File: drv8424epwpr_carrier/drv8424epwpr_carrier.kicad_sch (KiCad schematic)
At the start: 26 parts, among them J4 Conn_01x08, J5 Conn_01x08, U1 DRV8424EPWPR, U2 DMP4013LFG-7

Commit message: add footprint
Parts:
- CR1: footprint SOD123_DIO -> MMSZ5245B_7_F:SOD123_DIO
- C_SW1: renamed from C_SW; footprint CAPC340180_88N_KEM -> C1206C223J8RACTU:CAPC340180_88N_KEM
- C_VCP1: renamed from C_VCP; footprint CAPC340180_100N_KEM -> C1206C224K4RACTU:CAPC340180_100N_KEM
- C_VM1, C_VM2: footprint CAPC220145_88N_KEM -> C0805C103K8RACTU:CAPC220145_88N_KEM
- C_VM3, C_VM4: footprint EEE0GA101SR -> EEE-1AA101WR:EEE0GA101SR
- J4, J5: footprint (none) -> Connector_PinHeader_2.54mm:PinHeader_1x08_P2.54mm_Vertical
- LED1: footprint APHCM2012SYCK-F01:LED_APHCM2012SYCK-F01 -> APHCM2012SYCK_F01:LED_APHCM2012SYCK-F01
- LED2, LED4: footprint LED_APHCM2012CGCK-F01_KNB -> APHCM2012CGCK_F01:LED_APHCM2012CGCK-F01_KNB
- LED3, LED5: footprint APHCM2012SURCK-F01:LED_APHCM2012SURCK-F01 -> APHCM2012SURCK_F01:LED_APHCM2012SURCK-F01
- R1: footprint RC1206N_YAG -> RC1206FR_07100KL:RC1206N_YAG
- R1_REFA1: renamed from R1_REFA; footprint RC1206N_YAG -> RC1206FR_0747KL:RC1206N_YAG
- R1_REFB1: renamed from R1_REFB; footprint RC1206N_YAG -> RC1206FR_0747KL:RC1206N_YAG
- R2, R3, R4: footprint RC1206N_YAG -> RC1206FR_07590RL:RC1206N_YAG
- R2_REFA1: renamed from R2_REFA; footprint RC1206N_YAG -> RC1206FR_0716KL:RC1206N_YAG
- R2_REFB1: renamed from R2_REFB; footprint RC1206N_YAG -> RC1206FR_0716KL:RC1206N_YAG
- R_nFAULT1: renamed from R_nFAULT; footprint RC1206N_YAG -> RC1206FR_0710KL:RC1206N_YAG
- U1: footprint HTSSOP28_PWP_TEX -> DRV8424EPWPR:HTSSOP28_PWP_TEX
- U2: footprint SON8_DMP4013LFG-7_DIO -> DMP4013LFG_7:SON8_DMP4013LFG-7_DIO
- renumbered C_DVDD to C_DVDD1
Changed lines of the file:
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@@
 	(wire
 		(pts
+			(xy 124.46 80.01) (xy 124.46 78.74)
+		)
+		(stroke
+			(width 0)
+			(type default)
+		)
+	)
+	(wire
+		(pts
 			(xy 93.98 39.37) (xy 93.98 58.42)
 		)
@@
 			)
 		)
-		(property "Footprint" ""
+		(property "Footprint" "Connector_PinHeader_2.54mm:PinHeader_1x08_P2.54mm_Vertical"
 			(at 190.5 45.72 0)
 			(effects
@@
 			)
 		)
-		(property "Footprint" "LED_APHCM2012CGCK-F01_KNB"
+		(property "Footprint" "APHCM2012CGCK_F01:LED_APHCM2012CGCK-F01_KNB"
 			(at 58.42 125.73 0)
 			(effects
@@
 			)
 		)
-		(property "Footprint" "RC1206N_YAG"
+		(property "Footprint" "RC1206FR_07590RL:RC1206N_YAG"
 			(at 44.45 97.79 0)
 			(effects
@@
 		(dnp no)
 		(fields_autoplaced yes)
-		(property "Reference" "R2_REFB"
+		(property "Reference" "R2_REFB1"
 			(at 261.62 129.5399 90)
 			(effects
@@
 			)
 		)
-		(property "Footprint" "RC1206N_YAG"
+		(property "Footprint" "RC1206FR_0716KL:RC1206N_YAG"
 			(at 259.08 137.16 0)
 			(effects
@@
 			(project "drv8424epwpr_carrier"
 				(path "/ffaa5cf3-cedd-4f84-9f10-7046972ed335"
-					(reference "R2_REFB")
+					(reference "R2_REFB1")
 					(unit 1)
 				)
@@
 			)
 		)
-		(property "Footprint" "CAPC220145_88N_KEM"
+		(property "Footprint" "C0805C103K8RACTU:CAPC220145_88N_KEM"
 			(at 124.46 49.53 0)
 			(effects
@@
 			)
 		)
-		(property "Footprint" "EEE0GA101SR"
+		(property "Footprint" "EEE-1AA101WR:EEE0GA101SR"
 			(at -2.21 67.31 0)
 			(effects
@@
 			)
 		)
-		(property "Footprint" "EEE0GA101SR"
+		(property "Footprint" "EEE-1AA101WR:EEE0GA101SR"
 			(at 9.22 55.88 0)
 			(effects
@@
 		(dnp no)
 		(fields_autoplaced yes)
-		(property "Reference" "C_VCP"
+		(property "Reference" "C_VCP1"
 			(at 113.03 93.98 0)
 			(effects
@@
 			)
 		)
-		(property "Footprint" "CAPC340180_100N_KEM"
+		(property "Footprint" "C1206C224K4RACTU:CAPC340180_100N_KEM"
 			(at 116.84 100.33 0)
 			(effects
@@
 			(project ""
 				(path "/ffaa5cf3-cedd-4f84-9f10-7046972ed335"
-					(reference "C_VCP")
+					(reference "C_VCP1")
 					(unit 1)
 				)
@@
 			)
 		)
-		(property "Footprint" "APHCM2012SYCK-F01:LED_APHCM2012SYCK-F01"
+		(property "Footprint" "APHCM2012SYCK_F01:LED_APHCM2012SYCK-F01"
 			(at 135.89 50.8 0)
 			(effects
@@
 	(symbol
 		(lib_id "power:GND")
-		(at 124.46 78.74 0)
+		(at 124.46 80.01 0)
 		(unit 1)
 		(exclude_from_sim no)
@@
 		(fields_autoplaced yes)
 		(property "Reference" "#PWR08"
-			(at 124.46 85.09 0)
+			(at 124.46 86.36 0)
 			(effects
 				(font
@@
 		)
 		(property "Value" "GND"
-			(at 124.46 83.82 0)
+			(at 124.46 85.09 0)
 			(effects
 				(font
@@
 		)
 		(property "Footprint" ""
-			(at 124.46 78.74 0)
+			(at 124.46 80.01 0)
 			(effects
 				(font
@@
 		)
 		(property "Datasheet" ""
-			(at 124.46 78.74 0)
+			(at 124.46 80.01 0)
 			(effects
 				(font
@@
 		)
 		(property "Description" "Power symbol creates a global label with name \"GND\" , ground"
-			(at 124.46 78.74 0)
+			(at 124.46 80.01 0)
 			(effects
 				(font
@@
 			)
 		)
-		(property "Footprint" "HTSSOP28_PWP_TEX"
+		(property "Footprint" "DRV8424EPWPR:HTSSOP28_PWP_TEX"
 			(at 127 100.33 0)
 			(effects
@@
 			)
 		)
-		(property "Footprint" "SON8_DMP4013LFG-7_DIO"
+		(property "Footprint" "DMP4013LFG_7:SON8_DMP4013LFG-7_DIO"
 			(at 73.66 46.99 0)
 			(effects
@@
 		(on_board yes)
 		(dnp no)
-		(property "Reference" "C_DVDD"
+		(property "Reference" "C_DVDD1"
 			(at 167.894 142.494 90)
 			(effects
@@
 			(project ""
 				(path "/ffaa5cf3-cedd-4f84-9f10-7046972ed335"
-					(reference "C_DVDD")
+					(reference "C_DVDD1")
 					(unit 1)
 				)
@@
 			)
 		)
-		(property "Footprint" "SOD123_DIO"
+		(property "Footprint" "MMSZ5245B_7_F:SOD123_DIO"
 			(at 81.28 54.61 0)
 			(effects
@@
 			)
 		)
-		(property "Footprint" "RC1206N_YAG"
+		(property "Footprint" "RC1206FR_07590RL:RC1206N_YAG"
 			(at 44.45 125.73 0)
 			(effects
@@
 		(on_board yes)
 		(dnp no)
-		(property "Reference" "C_SW"
+		(property "Reference" "C_SW1"
 			(at 185.42 96.52 0)
 			(effects
@@
 			)
 		)
-		(property "Footprint" "CAPC340180_88N_KEM"
+		(property "Footprint" "C1206C223J8RACTU:CAPC340180_88N_KEM"
 			(at 181.61 102.87 0)
 			(effects
@@
 			(project ""
 				(path "/ffaa5cf3-cedd-4f84-9f10-7046972ed335"
-					(reference "C_SW")
+					(reference "C_SW1")
 					(unit 1)
 				)
@@
 		(dnp no)
 		(fields_autoplaced yes)
-		(property "Reference" "R1_REFA"
+		(property "Reference" "R1_REFA1"
 			(at 232.41 111.7599 90)
 			(effects
@@
 			)
 		)
-		(property "Footprint" "RC1206N_YAG"
+		(property "Footprint" "RC1206FR_0747KL:RC1206N_YAG"
 			(at 229.87 119.38 0)
 			(effects
@@
 			(project ""
 				(path "/ffaa5cf3-cedd-4f84-9f10-7046972ed335"
-					(reference "R1_REFA")
+					(reference "R1_REFA1")
 					(unit 1)
 				)
@@
 			)
 		)
-		(property "Footprint" "APHCM2012SURCK-F01:LED_APHCM2012SURCK-F01"
+		(property "Footprint" "APHCM2012SURCK_F01:LED_APHCM2012SURCK-F01"
 			(at 63.5 137.16 0)
 			(effects
@@
 			)
 		)
-		(property "Footprint" "RC1206N_YAG"
+		(property "Footprint" "RC1206FR_07590RL:RC1206N_YAG"
 			(at 135.89 73.66 0)
 			(effects
@@
 		(dnp no)
 		(fields_autoplaced yes)
-		(property "Reference" "R_nFAULT"
+		(property "Reference" "R_nFAULT1"
 			(at 199.39 123.1899 90)
 			(effects
@@
 			)
 		)
-		(property "Footprint" "RC1206N_YAG"
+		(property "Footprint" "RC1206FR_0710KL:RC1206N_YAG"
 			(at 196.85 130.81 0)
 			(effects
@@
 			(project ""
 				(path "/ffaa5cf3-cedd-4f84-9f10-7046972ed335"
-					(reference "R_nFAULT")
+					(reference "R_nFAULT1")
 					(unit 1)
 				)
@@
 		(dnp no)
 		(fields_autoplaced yes)
-		(property "Reference" "R1_REFB"
+		(property "Reference" "R1_REFB1"
 			(at 261.62 111.7599 90)
 			(effects
@@
 			)
 		)
-		(property "Footprint" "RC1206N_YAG"
+		(property "Footprint" "RC1206FR_0747KL:RC1206N_YAG"
 			(at 259.08 119.38 0)
 			(effects
@@
 			(project "drv8424epwpr_carrier"
 				(path "/ffaa5cf3-cedd-4f84-9f10-7046972ed335"
-					(reference "R1_REFB")
+					(reference "R1_REFB1")
 					(unit 1)
 				)
@@
 			)
 		)
-		(property "Footprint" "RC1206N_YAG"
+		(property "Footprint" "RC1206FR_07100KL:RC1206N_YAG"
 			(at 81.28 60.96 0)
 			(effects
@@
 			)
 		)
-		(property "Footprint" "LED_APHCM2012CGCK-F01_KNB"
+		(property "Footprint" "APHCM2012CGCK_F01:LED_APHCM2012CGCK-F01_KNB"
 			(at 58.42 97.79 0)
 			(effects
@@
 			)
 		)
-		(property "Footprint" ""
+		(property "Footprint" "Connector_PinHeader_2.54mm:PinHeader_1x08_P2.54mm_Vertical"
 			(at 227.33 45.72 0)
 			(effects
@@
 		(dnp no)
 		(fields_autoplaced yes)
-		(property "Reference" "R2_REFA"
+		(property "Reference" "R2_REFA1"
 			(at 232.41 129.5399 90)
 			(effects
@@
 			)
 		)
-		(property "Footprint" "RC1206N_YAG"
+		(property "Footprint" "RC1206FR_0716KL:RC1206N_YAG"
 			(at 229.87 137.16 0)
 			(effects
@@
 			(project ""
 				(path "/ffaa5cf3-cedd-4f84-9f10-7046972ed335"
-					(reference "R2_REFA")
+					(reference "R2_REFA1")
 					(unit 1)
 				)
@@
 			)
 		)
-		(property "Footprint" "APHCM2012SURCK-F01:LED_APHCM2012SURCK-F01"
+		(property "Footprint" "APHCM2012SURCK_F01:LED_APHCM2012SURCK-F01"
 			(at 63.5 109.22 0)
 			(effects
@@
 			)
 		)
-		(property "Footprint" "CAPC220145_88N_KEM"
+		(property "Footprint" "C0805C103K8RACTU:CAPC220145_88N_KEM"
 			(at 114.3 60.96 0)
 			(effects

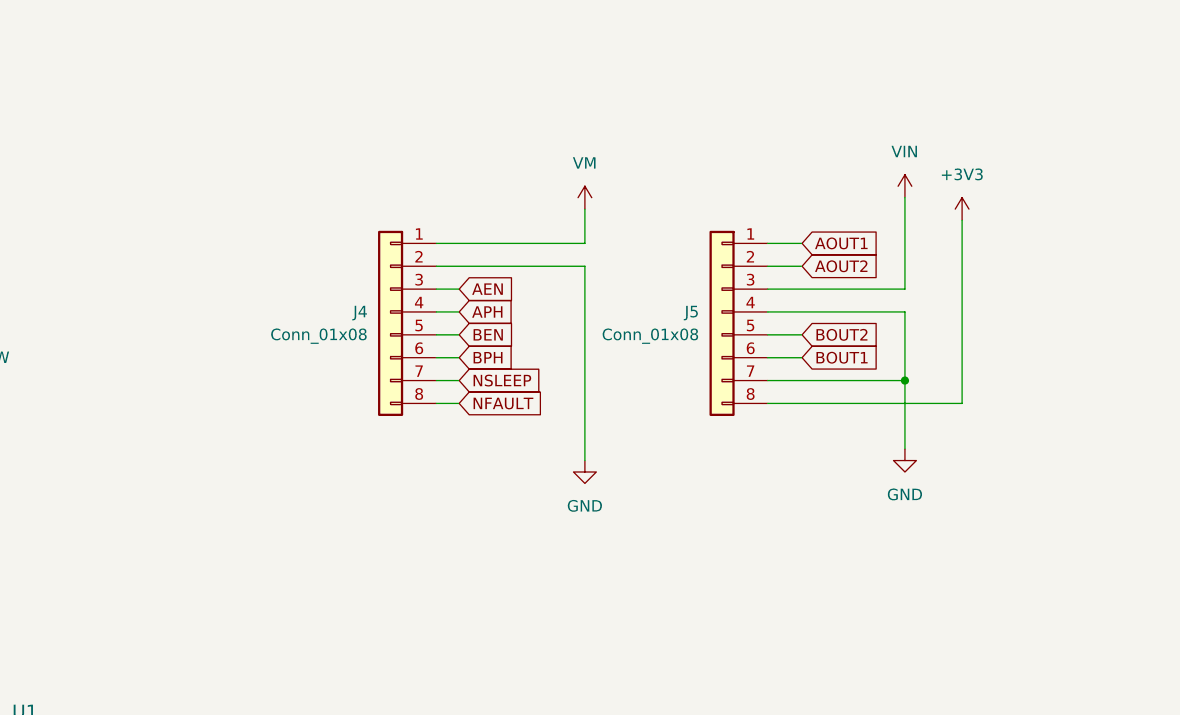
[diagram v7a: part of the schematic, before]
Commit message: update pin headers
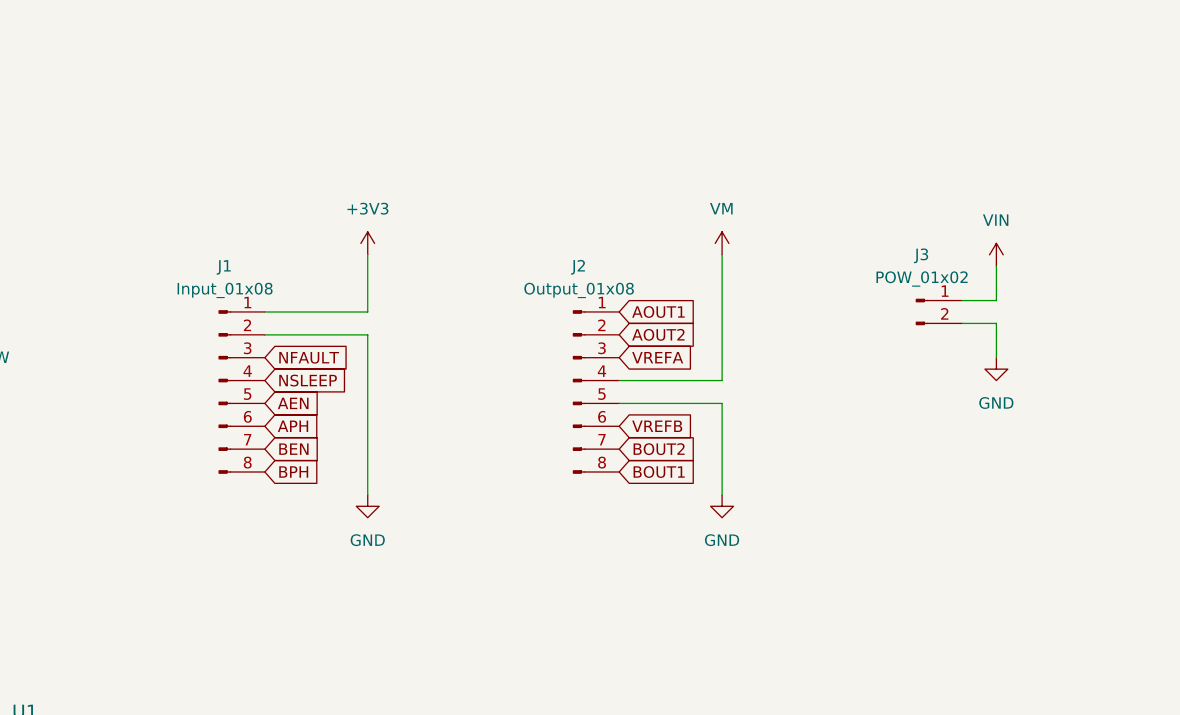
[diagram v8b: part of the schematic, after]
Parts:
- removed J4, J5: Conn_01x08, Connector_PinHeader_2.54mm:PinHeader_1x08_P2.54mm_Vertical, symbol Connector_Generic:Conn_01x08
- added J1: Input_01x08, Connector_PinHeader_2.54mm:PinHeader_1x08_P2.54mm_Vertical, symbol Connector:Conn_01x08_Pin
- added J2: Output_01x08, Connector_PinHeader_2.54mm:PinHeader_1x08_P2.54mm_Vertical, symbol Connector:Conn_01x08_Pin
- added J3: POW_01x02, Connector_PinHeader_2.54mm:PinHeader_1x02_P2.54mm_Horizontal, symbol Connector:Conn_01x02_Pin
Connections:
- net +3V3: now also J1.1 (Pin_1)
- net AEN: now also J1.5 (Pin_5)
- net AOUT1: now also J2.1 (Pin_1)
- net AOUT2: now also J2.2 (Pin_2)
- net APH: now also J1.6 (Pin_6)
- net BEN: now also J1.7 (Pin_7)
- net BOUT1: now also J2.8 (Pin_8)
- net BOUT2: now also J2.7 (Pin_7)
- net BPH: now also J1.8 (Pin_8)
- net GND: now also J1.2 (Pin_2), J2.5 (Pin_5), J3.2 (Pin_2)
- net NFAULT: now also J1.3 (Pin_3)
- net NSLEEP: now also J1.4 (Pin_4)
- net VIN: now also J3.1 (Pin_1)
- net VM: now also J2.4 (Pin_4)
- net VREFA: now also J2.3 (Pin_3)
- net VREFB: now also J2.6 (Pin_6)
